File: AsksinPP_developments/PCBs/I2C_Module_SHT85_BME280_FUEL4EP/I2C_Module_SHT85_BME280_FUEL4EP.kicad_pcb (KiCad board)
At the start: 2 copper layers, 30.5 x 17 mm, 14 parts, among them J1 Conn_01x04, J2 Conn_01x04, U1 BME280, U2 SHT85

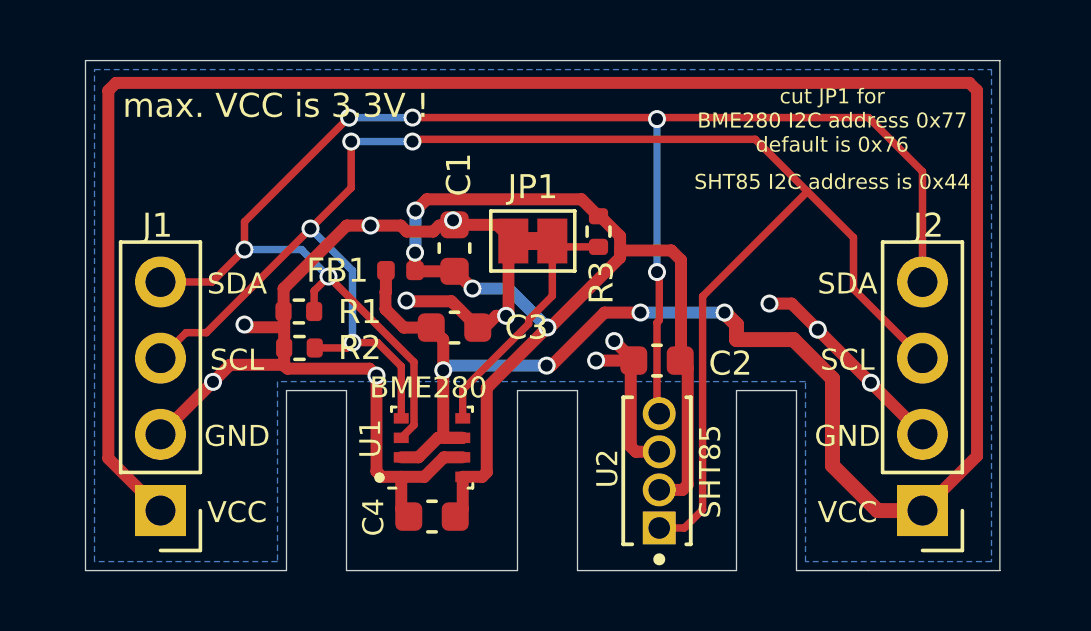
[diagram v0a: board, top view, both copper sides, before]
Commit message: PCB: I2C_Module_SHT85_BME280_FUEL4EP, I2C_Module_BME680_FUEL4EP: correction of connector placements in 3D view; 4Bit_I2C_Port_Expander_Module_FUEL4EP: change from 2N7000 to 2N7002K for SMD assembly
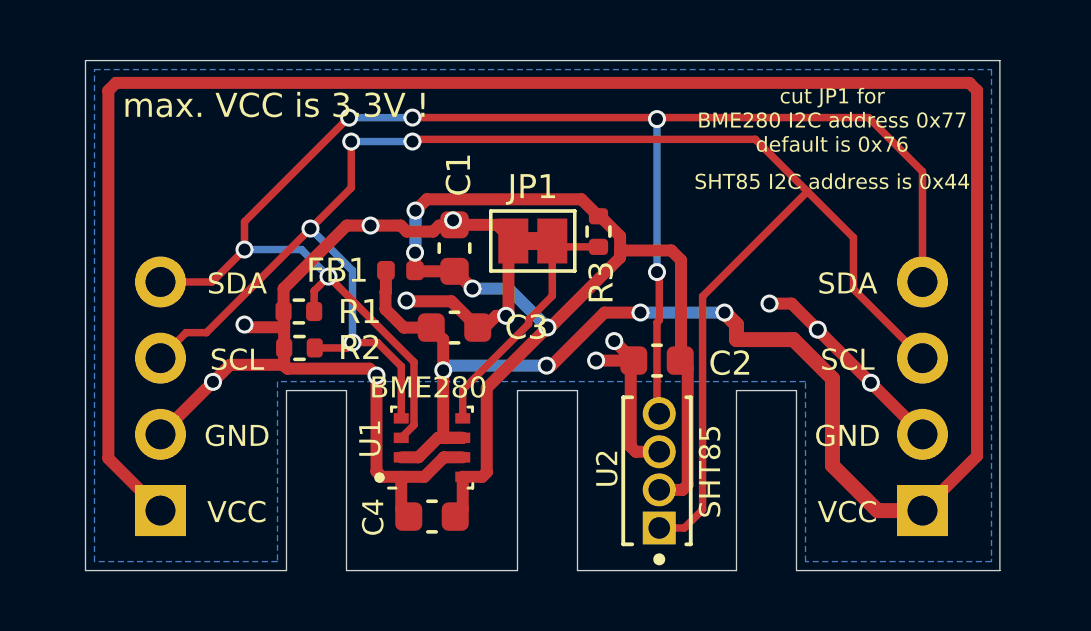
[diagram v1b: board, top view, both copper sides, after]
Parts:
- J1, J2: moved to B.Cu
- turned J1 to 0 degrees
- turned J2 to 0 degrees
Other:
- board text added: "SHT85 BME280 I2C Modul (C) FUEL4EP V1.1 12/2023"
- board text removed: "SHT85 BME280 I2C Modul (C) FUEL4EP V1.0 9/2023"

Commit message: PCBs: fix of I2C Pull-up resistors that were wrongly tied to GND
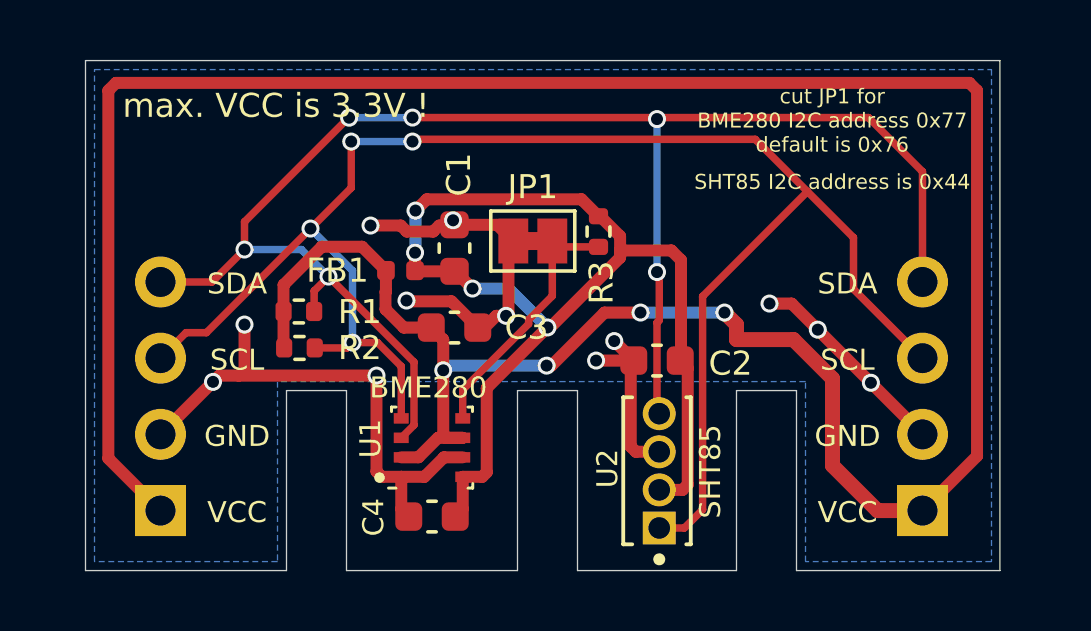
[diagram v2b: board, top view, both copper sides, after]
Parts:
- R1, R2: value 4.7k -> 10k
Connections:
- R1 pad 2: GND -> VCC
- R2 pad 2: GND -> VCC
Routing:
- net VCC: track 90.0 -> 96.4 mm
- net GND: track 47.9 -> 41.6 mm
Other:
- board text added: "SHT85 BME280 I2C Modul (C) FUEL4EP V1.2 02/2024"
- board text removed: "SHT85 BME280 I2C Modul (C) FUEL4EP V1.1 12/2023"
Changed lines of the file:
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@@
   (title_block
     (title "I2C_Module_SHT85_BME280_FUEL4EP")
-    (date "2023-12-15")
-    (rev "V1.1")
+    (date "2024-02-08")
+    (rev "V1.2")
     (company "(c) FUEL4EP")
   )
@@
     (descr "Resistor SMD 0402 (1005 Metric), square (rectangular) end terminal, IPC_7351 nominal, (Body size source: IPC-SM-782 page 72, https://www.pcb-3d.com/wordpress/wp-content/uploads/ipc-sm-782a_amendment_1_and_2.pdf), generated with kicad-footprint-generator")
     (tags "resistor")
-    (property "LCSC" "C25900")
+    (property "LCSC" "C25744")
     (property "Sheetfile" "I2C_Module_SHT85_BME280_FUEL4EP.kicad_sch")
     (property "Sheetname" "")
@@
       (effects (font (size 0.8 0.8) (thickness 0.15)))
     )
-    (fp_text value "4.7k" (at -0.12 -0.015) (layer "F.Fab")
+    (fp_text value "10k" (at -0.12 -0.015) (layer "F.Fab")
       (effects (font (size 0.8 0.8) (thickness 0.15)))
     )
@@
       (net 4 "/SDA") (pintype "passive"))
     (pad "2" smd roundrect (at 0.51 0 180) (size 0.54 0.64) (layers "F.Cu" "F.Paste" "F.Mask") (roundrect_rratio 0.25)
-      (net 2 "GND") (pintype "passive"))
+      (net 1 "VCC") (pintype "passive"))
     (model "${KICAD6_3DMODEL_DIR}/Resistor_SMD.3dshapes/R_0402_1005Metric.wrl"
       (offset (xyz 0 0 0))
@@
     (descr "Resistor SMD 0402 (1005 Metric), square (rectangular) end terminal, IPC_7351 nominal, (Body size source: IPC-SM-782 page 72, https://www.pcb-3d.com/wordpress/wp-content/uploads/ipc-sm-782a_amendment_1_and_2.pdf), generated with kicad-footprint-generator")
     (tags "resistor")
-    (property "LCSC" "C25900")
+    (property "LCSC" "C25744")
     (property "Sheetfile" "I2C_Module_SHT85_BME280_FUEL4EP.kicad_sch")
     (property "Sheetname" "")
@@
       (effects (font (size 0.8 0.8) (thickness 0.15)))
     )
-    (fp_text value "4.7k" (at -0.2 -0.1) (layer "F.Fab")
+    (fp_text value "10k" (at -0.2 -0.1) (layer "F.Fab")
       (effects (font (size 0.8 0.8) (thickness 0.15)))
     )
@@
       (net 3 "/SCL") (pintype "passive"))
     (pad "2" smd roundrect (at 0.51 0 180) (size 0.54 0.64) (layers "F.Cu" "F.Paste" "F.Mask") (roundrect_rratio 0.25)
-      (net 2 "GND") (pintype "passive"))
+      (net 1 "VCC") (pintype "passive"))
     (model "${KICAD6_3DMODEL_DIR}/Resistor_SMD.3dshapes/R_0402_1005Metric.wrl"
       (offset (xyz 0 0 0))
@@
   (gr_line (start 21.7 0) (end 16.4 0) (layer "Edge.Cuts") (width 0.0381))
   (gr_line (start 30.48 -17) (end 30.48 0) (layer "Edge.Cuts") (width 0.0381))
-  (gr_text "SHT85 BME280\nI2C Modul\n(C) FUEL4EP\nV1.1\n12/2023" (at 15.748 -9.144) (layer "B.SilkS")
+  (gr_text "SHT85 BME280\nI2C Modul\n(C) FUEL4EP\nV1.2\n02/2024" (at 15.748 -9.144) (layer "B.SilkS")
     (effects (font (size 0.7 0.7) (thickness 0.1524)) (justify mirror))
   )
@@
   (segment (start 29.718 -3.818) (end 27.9 -2) (width 0.4) (layer "F.Cu") (net 1))
   (segment (start 15.531258 -6.831258) (end 17.3 -8.6) (width 0.4) (layer "F.Cu") (net 1))
+  (segment (start 7.874 -10.795) (end 9.22 -10.795) (width 0.4) (layer "F.Cu") (net 1))
   (segment (start 29.464 -16.256) (end 29.718 -16.002) (width 0.4) (layer "F.Cu") (net 1))
   (segment (start 0.762 -3.738) (end 0.762 -16.002) (width 0.4) (layer "F.Cu") (net 1))
+  (segment (start 9.22 -10.795) (end 10.015 -10) (width 0.4) (layer "F.Cu") (net 1))
+  (segment (start 6.602 -9.523) (end 7.874 -10.795) (width 0.4) (layer "F.Cu") (net 1))
   (segment (start 10.0005 -8.710257) (end 10.610757 -8.1) (width 0.4) (layer "F.Cu") (net 1))
   (segment (start 10.0005 -9.289743) (end 10.0005 -8.710257) (width 0.4) (layer "F.Cu") (net 1))
@@
   (segment (start 10.015 -10) (end 10.015 -9.304243) (width 0.4) (layer "F.Cu") (net 1))
   (segment (start 11.925 -4.5) (end 11.925 -7.7) (width 0.4) (layer "F.Cu") (net 1))
+  (segment (start 6.602 -8.636) (end 6.602 -7.441) (width 0.4) (layer "F.Cu") (net 1))
   (segment (start 24.9 -3.5) (end 26.4 -2) (width 0.5) (layer "F.Cu") (net 1))
   (segment (start 0.762 -16.002) (end 1.016 -16.256) (width 0.4) (layer "F.Cu") (net 1))
   (segment (start 10.610757 -8.1) (end 11.525 -8.1) (width 0.4) (layer "F.Cu") (net 1))
+  (segment (start 6.602 -8.636) (end 6.602 -9.523) (width 0.4) (layer "F.Cu") (net 1))
   (segment (start 10.015 -9.304243) (end 10.0005 -9.289743) (width 0.4) (layer "F.Cu") (net 1))
   (segment (start 12 -4.425) (end 11.925 -4.5) (width 0.4) (layer "F.Cu") (net 1))
+  (segment (start 6.602 -7.441) (end 6.622 -7.421) (width 0.4) (layer "F.Cu") (net 1))
   (segment (start 24.9 -6.4) (end 23.6 -7.7) (width 0.5) (layer "F.Cu") (net 1))
   (segment (start 27.9 -2) (end 26.4 -2) (width 0.5) (layer "F.Cu") (net 1))
@@
   (segment (start 10.725 -8.975) (end 12.2 -8.975) (width 0.4) (layer "F.Cu") (net 2))
   (segment (start 10.525 -2.05) (end 10.775 -1.8) (width 0.4) (layer "F.Cu") (net 2))
+  (segment (start 5.3 -8.2) (end 5.3 -6.697) (width 0.4) (layer "F.Cu") (net 2))
   (segment (start 9.875 -3.125) (end 9.7 -3.3) (width 0.4) (layer "F.Cu") (net 2))
   (segment (start 14.1 -8.572728) (end 14.019014 -8.491742) (width 0.4) (layer "F.Cu") (net 2))
   (segment (start 9.7 -3.3) (end 9.7 -6.5) (width 0.4) (layer "F.Cu") (net 2))
-  (segment (start 6.602 -9.396) (end 6.602 -8.636) (width 0.4) (layer "F.Cu") (net 2))
   (segment (start 10.725 -8.975) (end 10.7 -9) (width 0.4) (layer "F.Cu") (net 2))
-  (segment (start 9.469 -6.731) (end 9.7 -6.5) (width 0.4) (layer "F.Cu") (net 2))
   (segment (start 10.510257 -11.5005) (end 9.5005 -11.5005) (width 0.4) (layer "F.Cu") (net 2))
   (segment (start 14.1 -10.825) (end 14.1 -8.572728) (width 0.4) (layer "F.Cu") (net 2))
   (segment (start 18.175 -4.132183) (end 18.347183 -3.96) (width 0.4) (layer "F.Cu") (net 2))
+  (segment (start 5.3 -6.697) (end 5.103 -6.5) (width 0.4) (layer "F.Cu") (net 2))
   (segment (start 13.691742 -8.491742) (end 14.019014 -8.491742) (width 0.4) (layer "F.Cu") (net 2))
   (segment (start 24.41 -8.03) (end 23.54 -8.9) (width 0.4) (layer "F.Cu") (net 2))
   (segment (start 17.02 -7) (end 18.275 -7) (width 0.4) (layer "F.Cu") (net 2))
-  (segment (start 6.622 -8.11) (end 5.39 -8.11) (width 0.4) (layer "F.Cu") (net 2))
+  (segment (start 9.7 -6.5) (end 5.103 -6.5) (width 0.4) (layer "F.Cu") (net 2))
   (segment (start 11.589743 -11.3005) (end 10.710257 -11.3005) (width 0.4) (layer "F.Cu") (net 2))
   (segment (start 10.525 -3.125) (end 10.525 -2.05) (width 0.4) (layer "F.Cu") (net 2))
-  (segment (start 6.731 -6.731) (end 9.469 -6.731) (width 0.4) (layer "F.Cu") (net 2))
   (segment (start 13.3 -8.1) (end 13.691742 -8.491742) (width 0.4) (layer "F.Cu") (net 2))
-  (segment (start 6.682 -6.78) (end 6.731 -6.731) (width 0.4) (layer "F.Cu") (net 2))
   (segment (start 12.2755 -11.5005) (end 11.789743 -11.5005) (width 0.4) (layer "F.Cu") (net 2))
-  (segment (start 5.39 -8.11) (end 5.3 -8.2) (width 0.4) (layer "F.Cu") (net 2))
-  (segment (start 6.622 -6.84) (end 6.682 -6.78) (width 0.4) (layer "F.Cu") (net 2))
+  (segment (start 4.46 -6.5) (end 4.25 -6.29) (width 0.4) (layer "F.Cu") (net 2))
+  (segment (start 5.103 -6.5) (end 4.46 -6.5) (width 0.4) (layer "F.Cu") (net 2))
   (segment (start 26.18 -6.26) (end 24.41 -8.03) (width 0.4) (layer "F.Cu") (net 2))
   (segment (start 23.54 -8.9) (end 22.8 -8.9) (width 0.4) (layer "F.Cu") (net 2))
   (segment (start 13.075 -8.1) (end 12.2 -8.975) (width 0.4) (layer "F.Cu") (net 2))
-  (segment (start 4.818 -6.858) (end 6.604 -6.858) (width 0.4) (layer "F.Cu") (net 2))
   (segment (start 11.789743 -11.5005) (end 11.589743 -11.3005) (width 0.4) (layer "F.Cu") (net 2))
   (segment (start 18.347183 -3.96) (end 19.125 -3.96) (width 0.4) (layer "F.Cu") (net 2))
   (segment (start 12.575 -3.775) (end 11.947822 -3.775) (width 0.4) (layer "F.Cu") (net 2))
-  (segment (start 6.622 -7.421) (end 6.622 -6.84) (width 0.4) (layer "F.Cu") (net 2))
   (segment (start 13.72 -11.525) (end 14.26 -10.985) (width 0.4) (layer "F.Cu") (net 2))
   (segment (start 10.525 -3.125) (end 9.875 -3.125) (width 0.4) (layer "F.Cu") (net 2))
   (segment (start 12.3 -11.525) (end 13.72 -11.525) (width 0.4) (layer "F.Cu") (net 2))
-  (segment (start 6.622 -8.11) (end 6.622 -8.616) (width 0.4) (layer "F.Cu") (net 2))
-  (segment (start 6.604 -6.858) (end 6.682 -6.78) (width 0.4) (layer "F.Cu") (net 2))
   (segment (start 18.275 -7) (end 17.625002 -7.65) (width 0.4) (layer "F.Cu") (net 2))
   (segment (start 11.297822 -3.125) (end 10.525 -3.125) (width 0.4) (layer "F.Cu") (net 2))
@@
   (segment (start 10.710257 -11.3005) (end 10.510257 -11.5005) (width 0.4) (layer "F.Cu") (net 2))
   (segment (start 2.5 -4.54) (end 4.25 -6.29) (width 0.4) (layer "F.Cu") (net 2))
-  (segment (start 8.7065 -11.5005) (end 6.602 -9.396) (width 0.4) (layer "F.Cu") (net 2))
-  (segment (start 9.5005 -11.5005) (end 8.7065 -11.5005) (width 0.4) (layer "F.Cu") (net 2))
   (segment (start 27.9 -4.54) (end 26.18 -6.26) (width 0.4) (layer "F.Cu") (net 2))
-  (segment (start 6.622 -7.421) (end 6.622 -8.11) (width 0.4) (layer "F.Cu") (net 2))
   (segment (start 18.175 -6.9) (end 18.175 -4.132183) (width 0.4) (layer "F.Cu") (net 2))
-  (segment (start 4.25 -6.29) (end 4.818 -6.858) (width 0.4) (layer "F.Cu") (net 2))
   (via (at 4.25 -6.29) (size 0.6) (drill 0.4) (layers "F.Cu" "B.Cu") (net 2))
   (via (at 17.625002 -7.65) (size 0.6) (drill 0.4) (layers "F.Cu" "B.Cu") (net 2))

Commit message: PCBs: upgrade some PCBs to KiCAD 7; fix of unnecessary leakage current of I2C address selector: I2C_Module_SHT85_BME280_FUEL4EP, I2C_Module_SHT45_BME280_small_FUEL4EP, I2C_Module_SHT45_BME280_FUEL4EP, I2C_Module_BME280_FUEL4EP, and I2C_Module_BME680_FUEL4EP
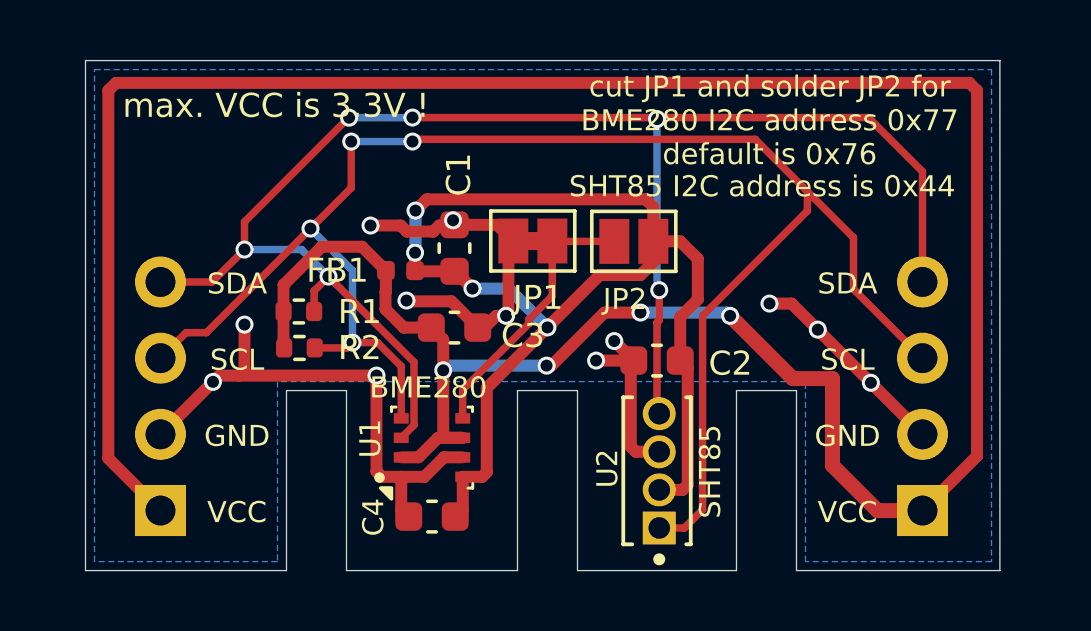
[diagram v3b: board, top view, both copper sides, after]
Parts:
- removed R3: 10k, Resistor_SMD:R_0402_1005Metric
- added JP2: SolderJumper_2_Open, Jumper:SolderJumper-2_P1.3mm_Open_Pad1.0x1.5mm, F.Cu at (18.3, -11.0)
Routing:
- net VDDA: track 37.4 -> 40.3 mm
- net Net-(JP1-B): track 8.49 -> 9.93 mm
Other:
- board text added: "SHT85 BME280 I2C Modul (C) FUEL4EP V1.3 04/2024"
- board text added: "cut JP1 and solder JP2 for BME280 I2C address 0x77 default is 0x76"
- board text removed: "SHT85 BME280 I2C Modul (C) FUEL4EP V1.2 02/2024"
- board text removed: "cut JP1 for BME280 I2C address 0x77 default is 0x76"

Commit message: PCBs/I2C_Module_SHT85_BME280: migration to KiCAD 8; fix of DRC rules
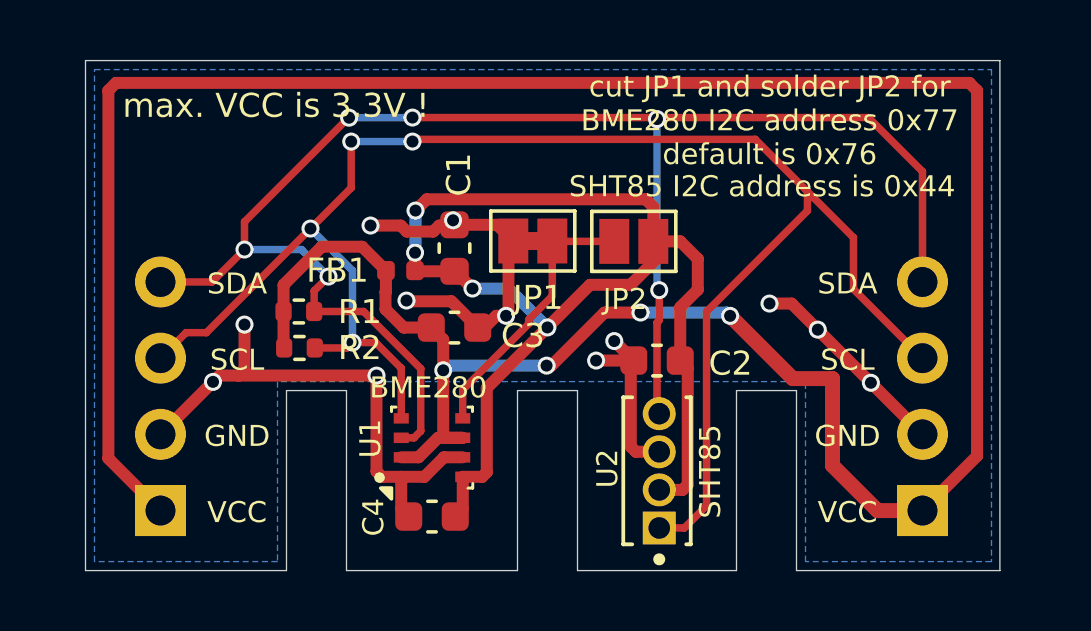
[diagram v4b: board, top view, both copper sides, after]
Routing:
- net Net-(JP1-B): track 9.93 -> 9.20 mm
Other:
- board text added: "SHT85 BME280 I2C Modul (C) FUEL4EP V1.4 09/2024"
- board text removed: "SHT85 BME280 I2C Modul (C) FUEL4EP V1.3 04/2024"
